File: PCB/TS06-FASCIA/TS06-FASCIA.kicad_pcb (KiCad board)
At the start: 2 copper layers, 0 parts

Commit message: TS06-FASCIA board: outline, placement, nets and front artwork
tools/mkpcb.py generates the board; tools/checkpcb.py checks it offline. Placement
and artwork only - no routing yet, on purpose. If a control sits 3mm off, routing it
first is wasted work.

FRONT FACE RULE, and it changed the design: nothing punches a hole through the face.
The first pass used through-hole axial resistors and through-hole landing pads, and
checkpcb caught why that was wrong - the decorative gold on the face is genuine copper
on F.Cu, so every through-hole pad it crossed was a short, not a graphic. Three of them
were. Rather than route the artwork around the pads, the pads left the front: every
wire-landing pad is now SMD on B.Cu and every passive is 1206 on B.Cu. The only holes
in the face are five bushings and four mounting screws, which is better product design
than the thing that forced it.

Board: 176 x 52 x 2.0mm, rounded 1.5mm corners, 13 nets, 42 pads.
Front carries the 30.00deg dial fan, gold ENIG numerals and the SUB supply rule.
Back carries R1-R8, J1 and the landing pads, all clear of the 25.00mm rotary keepout.

Two conventions the generator documents: every footprint is placed at rotation 0,
because KiCad stores rotated pad coordinates in a way that is easy to get subtly wrong
by hand; and back-side parts are authored directly on B.* layers rather than flipped,
so there is no mirror arithmetic to get wrong either.

Co-Authored-By: Claude Opus 5 <noreply@anthropic.com>
Claude-Session: https://claude.ai/code/session_01Wbajb7CU1SV8ZUPn3KkB8i
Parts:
- added ?: , MountingHole_2.7mm, F.Cu at (4.50, 4.50)
- added ?: , MountingHole_2.7mm, F.Cu at (171.5, 4.50)
- added ?: , MountingHole_2.7mm, F.Cu at (4.50, 47.5)
- added ?: , MountingHole_2.7mm, F.Cu at (171.5, 47.5)
- added J1: JST-XH 6, TS06_JST_XH_6, B.Cu at (158.0, 45.5)
- added R1: 4.7k 1%, TS06_R_1206_HandSolder, B.Cu at (20.0, 48.0)
- added R2: 4.7k 1%, TS06_R_1206_HandSolder, B.Cu at (26.5, 48.0)
- added R3: 4.7k 1%, TS06_R_1206_HandSolder, B.Cu at (33.0, 48.0)
- added R4: 4.7k 1%, TS06_R_1206_HandSolder, B.Cu at (39.5, 48.0)
- added R5: 4.7k 1%, TS06_R_1206_HandSolder, B.Cu at (46.0, 48.0)
- added R6: 10k, TS06_R_1206_HandSolder, B.Cu at (106.5, 8.50)
- added R7: 20k, TS06_R_1206_HandSolder, B.Cu at (95.0, 44.0)
- added R8: 10k, TS06_R_1206_HandSolder, B.Cu at (118.0, 44.0)
- added SW1: SR25 6-pos, TS06_Rotary_SR25_PanelMount, F.Cu at (30.0, 26.0)
- added SW2: FIELD, TS06_MT1_Lever_PanelMount, F.Cu at (95.0, 26.0)
- added SW3: SUB, TS06_MT1_Lever_PanelMount, F.Cu at (118.0, 26.0)
- added SW4: MINUS, TS06_KMD1_Button_PanelMount, F.Cu at (146.0, 26.0)
- added SW5: PLUS, TS06_KMD1_Button_PanelMount, F.Cu at (164.0, 26.0)
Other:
- board outline added: 176 x 52 mm
- board text added: "+"
- board text added: "-"
- board text added: "1"
- board text added: "2"
- board text added: "3"
- board text added: "4"
- board text added: "5"
- board text added: "6"
- board text added: "AMBIENT"
- board text added: "DISPLAY"
- board text added: "FIELD"
- board text added: "FORMAT/DATE"
- board text added: "INFO"
- board text added: "MODE"
- board text added: "NORMAL"
- board text added: "ROTARY BODY 25.00 KEEPOUT - BACK SIDE"
- board text added: "SET TIME"
- board text added: "SUB"

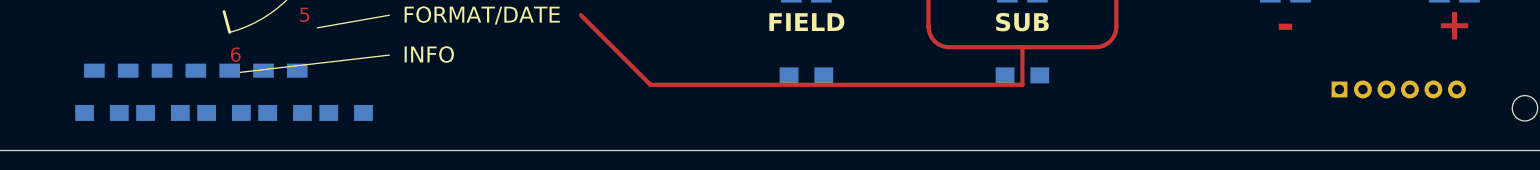
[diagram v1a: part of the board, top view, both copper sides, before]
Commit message: Strip fab notes, mirror back-side text, replace J1 with back-side cable pads
Three fixes from first contact with the board in KiCad.

Back-layer text was NOT mirrored - my mistake, not a viewer quirk. Renaming F.SilkS
to B.SilkS is not enough; KiCad needs (justify mirror) on every text that lives on a
back layer, or it reads backwards when you actually look at the back. 46 text blocks
corrected.

F.Fab notes stripped entirely. I had written long strings at fixed offsets inside
each footprint, so five copies of a 40mm note stacked into an unreadable pile the
moment they shared a board. The detail moves into each footprint's descr field, which
KiCad stores as metadata and never draws. Switch Value text is hidden too - a control
whose silk already says FIELD does not also need MT1 floating beside it. R1-R5 go
to 8.5mm spacing with 4k7 values so their labels stop colliding.

J1 is no longer a JST-XH. It is six back-side solder lands: a JST-XH is through-hole
only, so keeping it would have put six holes through the product's face - the one
thing this board is not allowed to do. The XH connector keeps its job at the MAIN
BOARD end, where the cable still unplugs for service. Only the fascia end is
permanent, and the fascia is not a serviceable part. Pad 1 carries a silk arrow and
the pinout is legended on B.Silkscreen. Strain relief is the chassis's job - nothing
on the board resists a pulled cable, and that needs to exist in the print.

Co-Authored-By: Claude Opus 5 <noreply@anthropic.com>
Claude-Session: https://claude.ai/code/session_01Wbajb7CU1SV8ZUPn3KkB8i
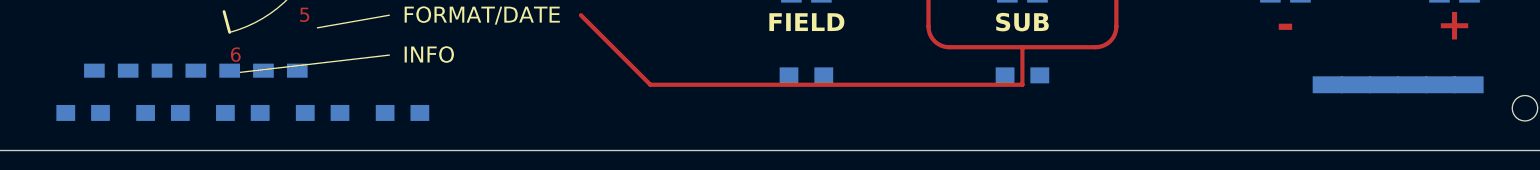
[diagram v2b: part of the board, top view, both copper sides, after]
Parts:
- J1: value JST-XH 6 -> CABLE 6; footprint TS06_JST_XH_6 -> TS06_CablePads_6
- R1, R2, R3, R4, R5: value 4.7k 1% -> 4k7
- moved R5 6.00 mm to (52.0, 48.0)
- moved R4 4.00 mm to (43.5, 48.0)
- moved R1 2.00 mm to (18.0, 48.0)
- moved R3 2.00 mm to (35.0, 48.0)
- moved J1 0.50 mm to (158.0, 45.0)
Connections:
- J1 pad 1: GND -> (no net)
- J1 pad 2: +5V -> (no net)
- J1 pad 3: A6 -> (no net)
- J1 pad 4: A7 -> (no net)
- J1 pad 5: D7 -> (no net)
- J1 pad 6: D8 -> (no net)
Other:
- board text added: "1 GND 2 +5V 3 A6 4 A7 5 D7 6 D8"
- board text added: "BODY 25.00"
- board text removed: "ROTARY BODY 25.00 KEEPOUT - BACK SIDE"

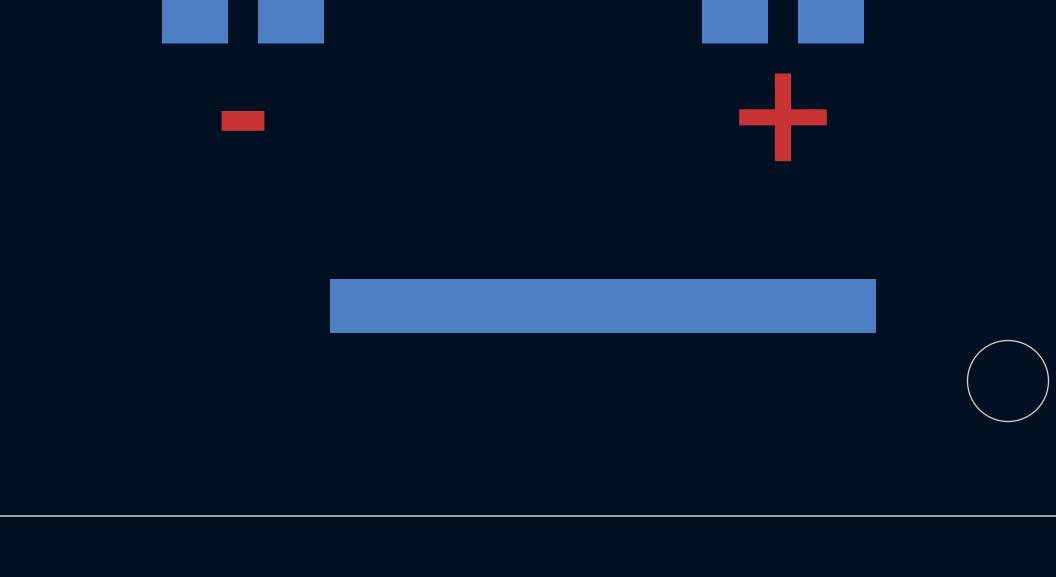
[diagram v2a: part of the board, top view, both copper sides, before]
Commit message: Fit the real JST PH SMT connector; fix nets that were silently not attaching
J1 becomes S6B-PH-SM4-TB: 6-way, 2.0mm pitch, side entry, surface mount, 2A/100V.
Land pattern taken from KiCad's Connector_JST library, which draws it from JST's
manufacturer drawing - not invented, and not scaled off a marketplace photo. JST's
own PH sheet omits the SMT layout entirely, so the library is the better source.

Cross-checked before use: the library body is 15.9mm wide, and JST's dimension table
gives B = A + 5.9 with A = 2.0 x (n-1), so n=6 is 10.0 + 5.9 = 15.9. Their table's
endpoints agree too (n=2 -> 7.9, n=16 -> 35.95). Two independent sources, one number.

Mirrored in X for back-side mounting, so pin 1 sits at +5 and numbering runs right to
left in board coordinates. A single-row connector is symmetric, so that is a valid
orientation rather than a workaround - but the pin-1 marker is mirrored with it. The
two MP pads are the retention tabs and carry the mechanical load; the signal pads do
not, which is why they are never optional.

BUG FIXED, and it was a bad one: netify only matched '(layers *.Cu *.Mask)', the
form through-hole pads emit. The moment the landing pads and connector became SMD with
explicit B.Cu layers, every net silently failed to attach - the board rendered
perfectly while being entirely unconnected. Now matches whatever layers a pad declares.
Verified against the schematic: 37 pads netted, 37 expected, every net member matching.

Co-Authored-By: Claude Opus 5 <noreply@anthropic.com>
Claude-Session: https://claude.ai/code/session_01Wbajb7CU1SV8ZUPn3KkB8i
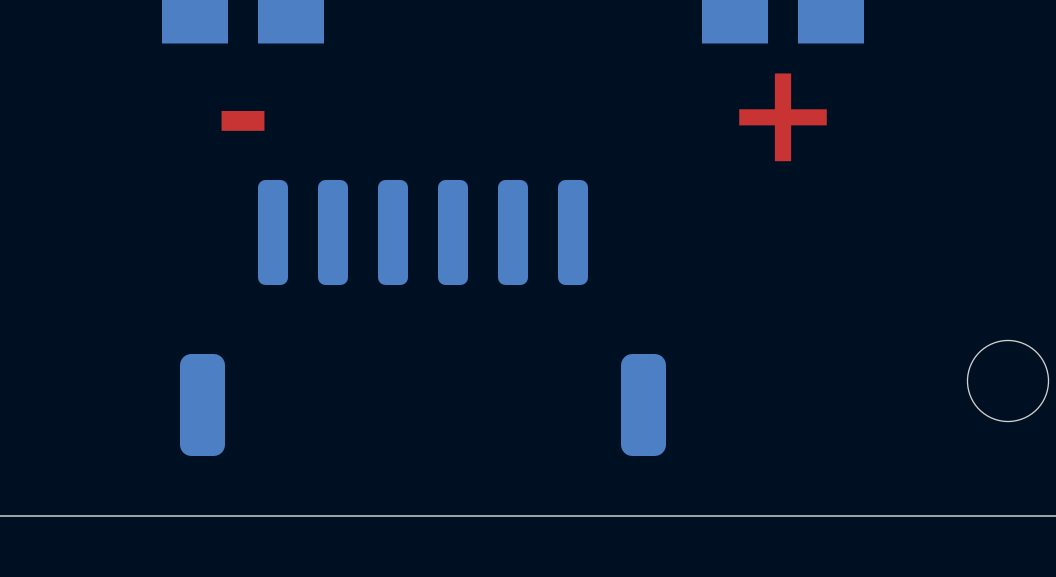
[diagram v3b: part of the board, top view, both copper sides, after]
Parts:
- J1: value CABLE 6 -> PH 6; footprint TS06_CablePads_6 -> TS06_JST_PH_S6B-PH-SM4-TB_Back
- moved J1 6.01 mm to (152.0, 45.4)
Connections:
- J1 pad 1: (no net) -> GND
- J1 pad 2: (no net) -> +5V
- J1 pad 3: (no net) -> A6
- J1 pad 4: (no net) -> A7
- J1 pad 5: (no net) -> D7
- J1 pad 6: (no net) -> D8
- R1 pad 1: (no net) -> TAP2
- R1 pad 2: (no net) -> GND
- R2 pad 1: (no net) -> TAP3
- R2 pad 2: (no net) -> TAP2
- R3 pad 1: (no net) -> TAP4
- R3 pad 2: (no net) -> TAP3
- R4 pad 1: (no net) -> TAP5
- R4 pad 2: (no net) -> TAP4
- R5 pad 1: (no net) -> +5V
- R5 pad 2: (no net) -> TAP5
- R6 pad 1: (no net) -> +5V
- R6 pad 2: (no net) -> A7
- R7 pad 1: (no net) -> LEVA
- R7 pad 2: (no net) -> GND
- R8 pad 1: (no net) -> LEVB
- R8 pad 2: (no net) -> GND
- SW1 pad 1: (no net) -> GND
- SW1 pad 2: (no net) -> TAP2
- SW1 pad 3: (no net) -> TAP3
- SW1 pad 4: (no net) -> TAP4
- SW1 pad 5: (no net) -> TAP5
- SW1 pad 6: (no net) -> +5V
- SW1 pad 7: (no net) -> A6
- SW2 pad 1: (no net) -> LEVA
- SW2 pad 2: (no net) -> A7
- SW3 pad 1: (no net) -> LEVB
- SW3 pad 2: (no net) -> A7
- SW4 pad 1: (no net) -> GND
- SW4 pad 2: (no net) -> D7
- SW5 pad 1: (no net) -> GND
- SW5 pad 2: (no net) -> D8

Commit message: Re-place the A6 ladder so it routes without a single crossing
The old arrangement had the rotary landing pads on a 3.6mm pitch in ascending order
and R1-R5 in a separate row to one side. Every tap trace then had to cross its
neighbours to reach the right pad - unroutable on one layer without vias.

Two changes fix it together. The landing pads go to 8mm pitch, which leaves room to
sit a 1206 in the gap between every adjacent pair. And both the pads and the chain
run in DESCENDING voltage order (+5V leftmost, GND, then COM on the right nearest
the connector), which puts each resistor's pad 1 - its higher node - facing left
toward the switch pad it belongs to.

The ladder is now ten short diagonals of 2 to 5mm, each one a switch pad flanked by
the two resistor pads that feed it, and no two can cross by construction:

  +5V   SW1.6(6.00)  R5.1(8.15)
  TAP5  R5.2(11.85)  SW1.5(14.00)  R4.1(16.15)
  TAP4  R4.2(19.85)  SW1.4(22.00)  R3.1(24.15)
  TAP3  R3.2(27.85)  SW1.3(30.00)  R2.1(32.15)
  TAP2  R2.2(35.85)  SW1.2(38.00)  R1.1(40.15)
  GND   R1.2(43.85)  SW1.1(46.00)

R6/R7/R8 also drop to a common y=40.5 in the clear band under the lever bodies so
the A7 and GND runs stay straight. Placement checks clean.

Co-Authored-By: Claude Opus 5 <noreply@anthropic.com>
Claude-Session: https://claude.ai/code/session_01Wbajb7CU1SV8ZUPn3KkB8i
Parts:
- moved R5 42.0 mm to (10.0, 48.0)
- moved R6 32.0 mm to (106.5, 40.5)
- moved R4 25.5 mm to (18.0, 48.0)
- moved R1 24.0 mm to (42.0, 48.0)
- moved R3 9.00 mm to (26.0, 48.0)
- moved R2 7.50 mm to (34.0, 48.0)
- moved R7 3.50 mm to (95.0, 40.5)
- moved R8 3.50 mm to (118.0, 40.5)
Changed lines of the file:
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@@
 		(layer "User.1")
 	)
-	(pad "1" smd rect
-		(at -10.8000 17.5000)
+	(pad "6" smd rect
+		(at -24.0000 17.5000)
 		(size 2.2 1.5)
 		(layers "B.Cu" "B.Mask")
-		(net 1 "GND")
-	)
-	(pad "2" smd rect
-		(at -7.2000 17.5000)
+		(net 2 "+5V")
+	)
+	(pad "5" smd rect
+		(at -16.0000 17.5000)
 		(size 2.2 1.5)
 		(layers "B.Cu" "B.Mask")
-		(net 7 "TAP2")
+		(net 10 "TAP5")
+	)
+	(pad "4" smd rect
+		(at -8.0000 17.5000)
+		(size 2.2 1.5)
+		(layers "B.Cu" "B.Mask")
+		(net 9 "TAP4")
 	)
 	(pad "3" smd rect
-		(at -3.6000 17.5000)
-		(size 2.2 1.5)
-		(layers "B.Cu" "B.Mask")
-		(net 8 "TAP3")
-	)
-	(pad "4" smd rect
 		(at 0.0000 17.5000)
 		(size 2.2 1.5)
 		(layers "B.Cu" "B.Mask")
-		(net 9 "TAP4")
-	)
-	(pad "5" smd rect
-		(at 3.6000 17.5000)
+		(net 8 "TAP3")
+	)
+	(pad "2" smd rect
+		(at 8.0000 17.5000)
 		(size 2.2 1.5)
 		(layers "B.Cu" "B.Mask")
-		(net 10 "TAP5")
-	)
-	(pad "6" smd rect
-		(at 7.2000 17.5000)
+		(net 7 "TAP2")
+	)
+	(pad "1" smd rect
+		(at 16.0000 17.5000)
 		(size 2.2 1.5)
 		(layers "B.Cu" "B.Mask")
-		(net 2 "+5V")
+		(net 1 "GND")
 	)
 	(pad "7" smd rect
-		(at 10.8000 17.5000)
+		(at 24.0000 17.5000)
 		(size 2.2 1.5)
 		(layers "B.Cu" "B.Mask")
@@
 	(generator_version "10.0")
 	(layer "B.Cu")
-	(at 18.0000 48.0000)
+	(at 10.0000 48.0000)
 	(descr "1206 chip resistor, hand-solder lands, authored on the back layers. The fascia's front is the product face, so no passive puts a hole through it.")
 	(tags "resistor 1206 SMD TERMINAL-06")
 	(attr through_hole)
-	(property "Reference" "R1"
+	(property "Reference" "R5"
 		(at 0 -2.2 0)
 		(layer "B.SilkS")
@@
 		(size 2.0 1.7)
 		(layers "B.Cu" "B.Mask")
-		(net 7 "TAP2")
+		(net 2 "+5V")
 	)
 	(pad "2" smd rect
@@
 		(size 2.0 1.7)
 		(layers "B.Cu" "B.Mask")
-		(net 1 "GND")
+		(net 10 "TAP5")
 	)
 	(fp_line
@@
 	(generator_version "10.0")
 	(layer "B.Cu")
-	(at 26.5000 48.0000)
+	(at 18.0000 48.0000)
 	(descr "1206 chip resistor, hand-solder lands, authored on the back layers. The fascia's front is the product face, so no passive puts a hole through it.")
 	(tags "resistor 1206 SMD TERMINAL-06")
 	(attr through_hole)
-	(property "Reference" "R2"
+	(property "Reference" "R4"
 		(at 0 -2.2 0)
 		(layer "B.SilkS")
@@
 		(size 2.0 1.7)
 		(layers "B.Cu" "B.Mask")
-		(net 8 "TAP3")
+		(net 10 "TAP5")
 	)
 	(pad "2" smd rect
@@
 		(size 2.0 1.7)
 		(layers "B.Cu" "B.Mask")
-		(net 7 "TAP2")
+		(net 9 "TAP4")
 	)
 	(fp_line
@@
 	(generator_version "10.0")
 	(layer "B.Cu")
-	(at 35.0000 48.0000)
+	(at 26.0000 48.0000)
 	(descr "1206 chip resistor, hand-solder lands, authored on the back layers. The fascia's front is the product face, so no passive puts a hole through it.")
 	(tags "resistor 1206 SMD TERMINAL-06")
@@
 	(generator_version "10.0")
 	(layer "B.Cu")
-	(at 43.5000 48.0000)
+	(at 34.0000 48.0000)
 	(descr "1206 chip resistor, hand-solder lands, authored on the back layers. The fascia's front is the product face, so no passive puts a hole through it.")
 	(tags "resistor 1206 SMD TERMINAL-06")
 	(attr through_hole)
-	(property "Reference" "R4"
+	(property "Reference" "R2"
 		(at 0 -2.2 0)
 		(layer "B.SilkS")
@@
 		(size 2.0 1.7)
 		(layers "B.Cu" "B.Mask")
-		(net 10 "TAP5")
+		(net 8 "TAP3")
 	)
 	(pad "2" smd rect
@@
 		(size 2.0 1.7)
 		(layers "B.Cu" "B.Mask")
-		(net 9 "TAP4")
+		(net 7 "TAP2")
 	)
 	(fp_line
@@
 	(generator_version "10.0")
 	(layer "B.Cu")
-	(at 52.0000 48.0000)
+	(at 42.0000 48.0000)
 	(descr "1206 chip resistor, hand-solder lands, authored on the back layers. The fascia's front is the product face, so no passive puts a hole through it.")
 	(tags "resistor 1206 SMD TERMINAL-06")
 	(attr through_hole)
-	(property "Reference" "R5"
+	(property "Reference" "R1"
 		(at 0 -2.2 0)
 		(layer "B.SilkS")
@@
 		(size 2.0 1.7)
 		(layers "B.Cu" "B.Mask")
-		(net 2 "+5V")
+		(net 7 "TAP2")
 	)
 	(pad "2" smd rect
@@
 		(size 2.0 1.7)
 		(layers "B.Cu" "B.Mask")
-		(net 10 "TAP5")
+		(net 1 "GND")
 	)
 	(fp_line
@@
 	(generator_version "10.0")
 	(layer "B.Cu")
-	(at 106.5000 8.5000)
+	(at 95.0000 40.5000)
 	(descr "1206 chip resistor, hand-solder lands, authored on the back layers. The fascia's front is the product face, so no passive puts a hole through it.")
 	(tags "resistor 1206 SMD TERMINAL-06")
 	(attr through_hole)
-	(property "Reference" "R6"
+	(property "Reference" "R7"
 		(at 0 -2.2 0)
 		(layer "B.SilkS")
@@
 		)
 	)
-	(property "Value" "10k"
+	(property "Value" "20k"
 		(at 0 2.2 0)
 		(layer "B.Fab")
@@
 		(size 2.0 1.7)
 		(layers "B.Cu" "B.Mask")
-		(net 2 "+5V")
+		(net 11 "LEVA")
 	)
 	(pad "2" smd rect
@@
 		(size 2.0 1.7)
 		(layers "B.Cu" "B.Mask")
-		(net 4 "A7")
+		(net 1 "GND")
 	)
 	(fp_line
@@
 	(generator_version "10.0")
 	(layer "B.Cu")
-	(at 95.0000 44.0000)
+	(at 106.5000 40.5000)
 	(descr "1206 chip resistor, hand-solder lands, authored on the back layers. The fascia's front is the product face, so no passive puts a hole through it.")
 	(tags "resistor 1206 SMD TERMINAL-06")
 	(attr through_hole)
-	(property "Reference" "R7"
+	(property "Reference" "R6"
 		(at 0 -2.2 0)
 		(layer "B.SilkS")
@@
 		)
 	)
-	(property "Value" "20k"
+	(property "Value" "10k"
 		(at 0 2.2 0)
 		(layer "B.Fab")
@@
 		(size 2.0 1.7)
 		(layers "B.Cu" "B.Mask")
-		(net 11 "LEVA")
+		(net 2 "+5V")
 	)
 	(pad "2" smd rect
@@
 		(size 2.0 1.7)
 		(layers "B.Cu" "B.Mask")
-		(net 1 "GND")
+		(net 4 "A7")
 	)
 	(fp_line
@@
 	(generator_version "10.0")
 	(layer "B.Cu")
-	(at 118.0000 44.0000)
+	(at 118.0000 40.5000)
 	(descr "1206 chip resistor, hand-solder lands, authored on the back layers. The fascia's front is the product face, so no passive puts a hole through it.")
 	(tags "resistor 1206 SMD TERMINAL-06")
